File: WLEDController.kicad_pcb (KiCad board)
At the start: 2 copper layers, 100 x 96 mm, 69 parts, among them J1 5V Power, J2 I2S EXTENSION, J3 LED Channel 1, J4 LED Channel 2, J5 LED Channel 3, J6 LED Channel 4, K1 SANYOU SRD, Q1 AOD403, Q2 IRLL2705, U1 AMS1117-3.3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

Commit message: Cleanup
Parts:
- U3: value esp32-wemos-d1-mini -> mini ESP32
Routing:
- added copper zone on F.Cu, net (none)

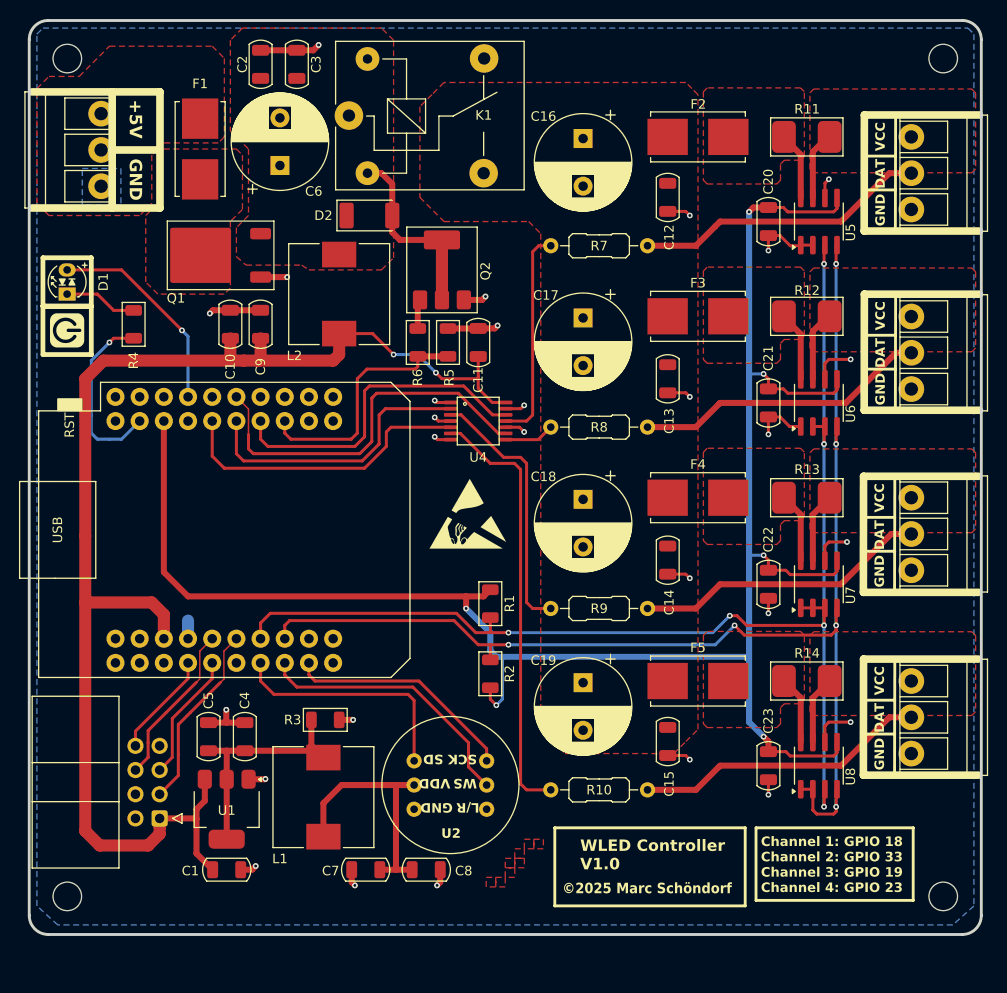
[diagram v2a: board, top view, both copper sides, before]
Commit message: Added Touch sensor
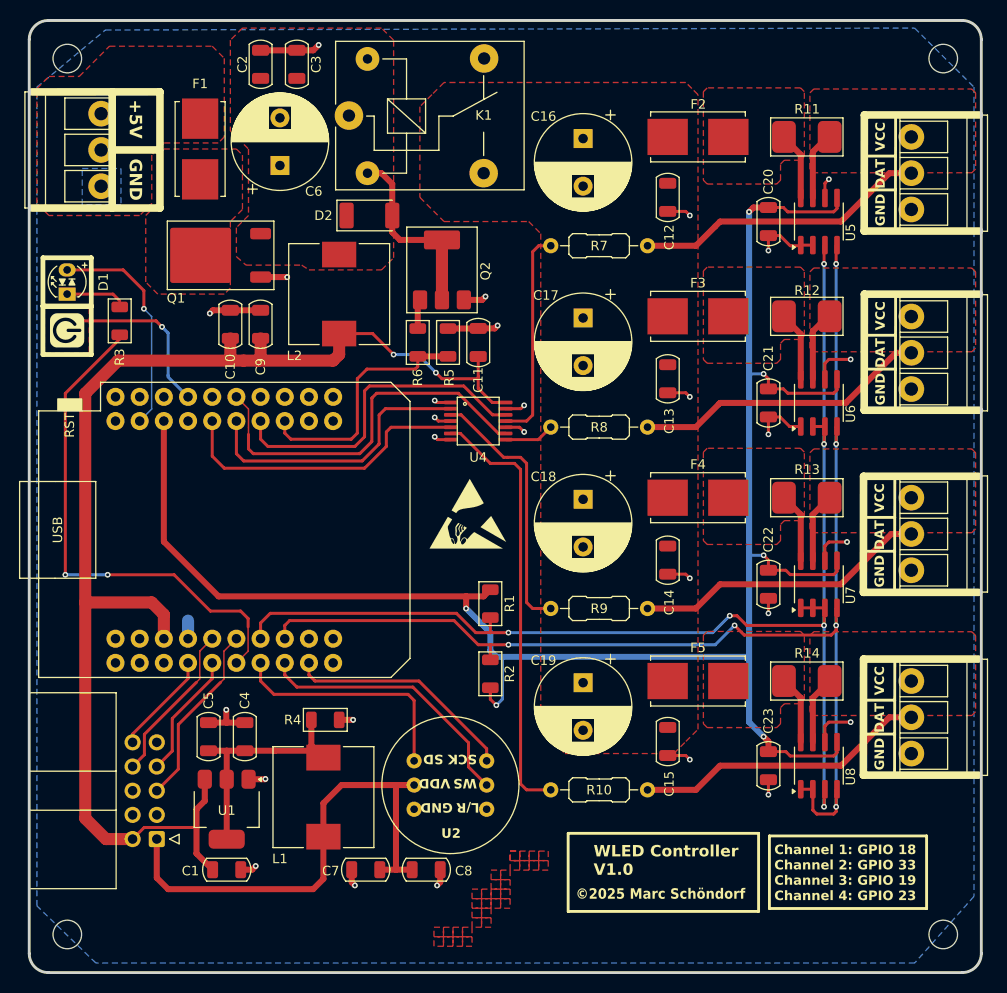
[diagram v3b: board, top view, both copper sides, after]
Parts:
- J2: value I2S EXTENSION -> I2S Extension; footprint Connector_IDC:IDC-Header_2x04_P2.54mm_Horizontal -> Connector_IDC:IDC-Header_2x05_P2.54mm_Horizontal
- U3: value mini ESP32 -> esp32-wemos-d1-mini
- moved J2 2.19 mm to (107.4, 137.0)
- moved R3 1.50 mm to (103.5, 82.5)
- renumbered R4 to R3, R3 to R4
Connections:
- J2 pad 1: +5V_D -> +3.3V_D
- J2 pad 2: GND -> +5V_D
- J2 pad 3: DOUT -> GND
- J2 pad 5: BCK -> DOUT
- J2 pad 6: LRCK -> GND
- J2 pad 7: GND -> BCK
- J2 pad 8: MCK -> LRCK
- R3 pad 1: Net-(U3-IO_13/TCK) -> Net-(U3-IO_12/TDI)
- U3 pad 13: Net-(D1-AK) -> TOUCH
- U3 pad 18: Net-(U3-IO_13/TCK) -> Net-(D1-AK)
- U3 pad 30: unconnected-(U3-IO_12/TDI-Pad30) -> Net-(U3-IO_12/TDI)
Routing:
- net Net-(U3-IO_12/TDI): track 0.00 -> 53.8 mm, vias 0 -> 2
- net +3.3V_D: track 26.1 -> 53.1 mm
- net Net-(U3-IO_13/TCK): track 19.2 -> 0.00 mm, vias 1 -> 0
- net TOUCH: track 0.00 -> 17.0 mm, vias 0 -> 1
- net +5V_D: track 142.3 -> 138.4 mm
- net +3.3V_ESP: track 194.1 -> 192.3 mm
- net Net-(D1-KA): track 7.69 -> 5.82 mm
- net Net-(D1-AK): track 21.9 -> 23.5 mm
- added copper zone on F.Cu, net TOUCH
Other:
- board size 100 x 96 mm -> 100 x 100 mm
